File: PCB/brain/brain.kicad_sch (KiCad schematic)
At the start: 108 parts, among them J1 Screw_Terminal_01x02, J2 Conn_01x04, Q1 CSD17577Q3A, Q2 CSD17577Q3A, U1 ESP32-S3-WROOM-1, U10 MAX17049G+T10, U11 AP64501SP-13, U2 TMC2209-LA, U3 W5500, U4 MAX98357A, U5 USBLC6-2SC6, U6 AP2112K-3.3, U7 R5460N214AF-TR-FE, U8 CH221K, U9 BQ25792

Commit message: commit
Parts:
- added C48: 22uF, symbol Device:C
- added R27: 115k, Resistor_SMD:R_0603_1608Metric, symbol Device:R
- added R28: 22.1k, Resistor_SMD:R_0603_1608Metric, symbol Device:R
- C42: value 10uF -> 22uF
- C43: value 0.1uF -> 22uF
- L2: value L -> 3.6uH
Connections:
- net GND: now also R28.2
- net at C42.1, C43.1: now also C48.1
- net 5VHP: now reaches C42.2, C43.2
- net 5VHP: now also L2.2, C48.2, R27.1
- net at U11.5 (FB): now also R27.2, R28.1

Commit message: ethernet
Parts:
- removed U6: AP2112K-3.3, Package_TO_SOT_SMD:SOT-23-5, symbol Regulator_Linear:AP2112K-3.3
- added C49, C50, C57, C58: 22uF, symbol Device:C
- added C51, C56, C59, C62, C64, C65, C66, C67, C68, C69, C82: 0.1uF, symbol Device:C
- added C52, C53, C54, C55, C60, C61, C63, C81: 10uF, symbol Device:C
- added C70: 15pF, Capacitor_SMD:C_0603_1608Metric, symbol Device:C
- added C71: 15PF, Capacitor_SMD:C_0603_1608Metric, symbol Device:C
- added C72: 22nF, symbol Device:C
- added C73, C74: 6.8nF, symbol Device:C
- added C75, C76: 10nF, symbol Device:C
- added C77: 4.7uF, symbol Device:C
- added C78: 1nF/2kV, Capacitor_SMD:C_1206_3216Metric, symbol Device:C
- added FB1, FB2: FerriteBead, Inductor_SMD:L_0603_1608Metric, symbol Device:FerriteBead
- added FB3: CBW160808U601T, Inductor_SMD:L_0603_1608Metric, symbol Device:FerriteBead
- added J3: RJ45_Hanrun_HR911105A_Horizontal, Connector_RJ:RJ45_Hanrun_HR911105A_Horizontal, symbol Connector:RJ45_Hanrun_HR911105A_Horizontal
- added J4, J5, J6: Conn_01x04, Connector_JST:JST_XH_B4B-XH-A_1x04_P2.50mm_Vertical, symbol Connector_Generic:Conn_01x04
- added J7, J8: Conn_01x06, Connector_PinSocket_2.54mm:PinSocket_1x06_P2.54mm_Vertical, symbol Connector_Generic:Conn_01x06
- added JP1: Jumper_3_Open, Connector_PinHeader_2.54mm:PinHeader_1x03_P2.54mm_Vertical, symbol Jumper:Jumper_3_Open
- added L3, L4: 4.7uH, easyeda2kicad:IND-SMD_L5.0-W5.0, symbol Device:L
- added LS1: Speaker, symbol Device:Speaker
- added R29: 10k, Resistor_SMD:R_0603_1608Metric, symbol Device:R
- added R30: 1M, symbol Device:R
- added R31, R32, R34, R35: 49.9R, Resistor_SMD:R_0603_1608Metric, symbol Device:R
- added R33: 10R, Resistor_SMD:R_0603_1608Metric, symbol Device:R
- added R36, R37: 300R, Resistor_SMD:R_0603_1608Metric, symbol Device:R
- added R38: 12.4k, Resistor_SMD:R_0603_1608Metric, symbol Device:R
- added R39: 1M, Resistor_SMD:R_0603_1608Metric, symbol Device:R
- added U12: AP63205WU, Package_TO_SOT_SMD:TSOT-23-6, symbol Regulator_Switching:AP63205WU
- added U14: AP63203WU, Package_TO_SOT_SMD:TSOT-23-6, symbol Regulator_Switching:AP63203WU
- added Y1: 25MHz, Crystal:Crystal_SMD_3225-4Pin_3.2x2.5mm, symbol Device:Crystal_GND24
- C5, C6: value 10uF -> 220pF
- L2: value 3.6uH -> 3.3uH; footprint (none) -> easyeda2kicad:IND-SMD_L11.5-W10.0_SMMS1040; LCSC Part (none) -> C149592
- R27: value 115k -> 52.3k
- R28: value 22.1k -> 10k
- U3: LCSC Part (none) -> C32843
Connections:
- net +3.3V: now also U3.28 (VDD), C57.2, C58.2, C61.2, C62.2, C81.2, C82.2, FB3.1, J3.12, J3.9, J8.2 (Pin_2), J8.3 (Pin_3), JP1.1 (A), L4.2, R29.2, U14.1 (FB); no longer C5.2
- net +5V: now also C49.2, C50.2, J4.1 (Pin_1), J5.1 (Pin_1), J6.1 (Pin_1), JP1.3 (B), L3.2, U12.1 (FB); no longer C6.2, U5.5 (VBUS)
- net ALRT: now also R29.1
- net GND: now also C42.1, C43.1, C48.1, C5.2, C6.2, U3.14 (AGND), U3.16 (AGND), U3.19 (AGND), U3.29 (GND), U3.3 (AGND), U3.48 (AGND), U3.9 (AGND), U4.11 (GND), U4.15 (GND), U4.17 (PAD), U4.3 (GND), C49.1, C50.1, C52.1, C53.1, C54.1, C55.1, C57.1, C58.1, C59.2, C60.2, C61.1, C62.1, C63.1, C64.1, C65.1, C66.1, C67.1, C68.1, C69.1, C70.2, C71.2, C72.1, C75.1, C76.1, C77.1, C78.1, C81.1, C82.1, J3.8, J4.4 (Pin_4), J5.4 (Pin_4), J6.4 (Pin_4), J7.1 (Pin_1), J7.2 (Pin_2), J8.1 (Pin_1), R38.2, U12.4 (GND), U14.4 (GND), Y1.2 (G), Y1.4 (G); no longer C5.1, C6.1
- net SCL: now also J4.3 (Pin_3), J5.3 (Pin_3), J6.3 (Pin_3)
- net SDA: now also J4.2 (Pin_2), J5.2 (Pin_2), J6.2 (Pin_2)
- net VSYS: now also C52.2, C53.2, C54.2, C55.2, U12.3 (IN), U14.2 (EN), U14.3 (IN)
- net DIN: now reaches U4.1 (DIN)
- net at U4.10 (OUTN): now also FB2.1
- net LRCLK: now reaches U4.14 (LRCLK)
- net BCLK: now reaches U4.16 (BCLK)
- net at U4.4 (~{SD_MODE}): now also R30.1
- net AMP_VDD: now reaches U4.7 (VDD), U4.8 (VDD)
- net AMP_VDD: now also C59.1, C60.1, JP1.2 (C), R30.2
- net at U4.9 (OUTP): now also FB1.1
- net at U3.1 (TXN): now also J3.2 (TD-), R32.2
- net at U3.10 (EXRES1): now also R38.1
- net +3.3VA: now reaches U3.11 (AVDD), U3.15 (AVDD), U3.17 (AVDD), U3.21 (AVDD), U3.4 (AVDD), U3.8 (AVDD)
- net +3.3VA: now also C63.2, C64.2, C65.2, C66.2, C67.2, C68.2, C69.2, FB3.2, R31.1, R32.1, R33.1
- net at U3.2 (TXP): now also J3.1 (TD+), R31.2
- net at U3.20 (TOCAP): now also C77.2
- net at U3.22 (1V2O): now also C76.2
- net LINKLED: now reaches U3.25 (LINKLED)
- net LINKLED: now also R36.2
- net ACTLED: now reaches U3.27 (ACTLED)
- net ACTLED: now also R37.2
- net at U3.30 (XI/CLKIN): now also C71.1, R39.1, Y1.1
- net at U3.31 (XO): now also C70.1, R39.2, Y1.3
- net SCSn: now reaches U3.32 (~{SCS})
- net SCLK: now reaches U3.33 (SCLK)
- net SCLK: now also J7.4 (Pin_4)
- net MISO: now reaches U3.34 (MISO)
- net MISO: now also J8.6 (Pin_6)
- net MOSI: now reaches U3.35 (MOSI)
- net MOSI: now also J7.3 (Pin_3)
- net INTn: now reaches U3.36 (~{INT})
- net INTn: now also J7.6 (Pin_6)
- net RSTn: now reaches U3.37 (~{RST})
- net RSTn: now also J8.5 (Pin_5)
- net PMODE2: now reaches U3.43 (PMODE2)
- net PMODE1: now reaches U3.44 (PMODE1)
- net PMODE0: now reaches U3.45 (PMODE0)
- net at U3.5 (RXN): now also C74.2, R34.1
- net at U3.6 (RXP): now also C73.2, R35.1
- new net: C73.1, J3.3 (RD+)
- new net: C5.1, FB2.2, LS1.2
- new net: C75.2, J3.5 (RCT), R34.2, R35.2
- new net: C56.1, U14.6 (BST)
- new net: C56.2, L4.1, U14.5 (SW)
- new net: C51.2, L3.1, U12.5 (SW)
- new net: C51.1, U12.6 (BST)
- new net: C6.1, FB1.2, LS1.1
- new net: C74.1, J3.6 (RD-)
- new net: J3.10, R37.1
- new net: C72.2, J3.4 (TCT), R33.2
- new net: J3.11, R36.1
- new net 5V_EN: U12.2 (EN)
- new net CGND: C78.2, J3.SH
- new net EthCS: J7.5 (Pin_5)
- no-connect marks 6 -> 17
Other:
- note added: "3.3V Buck"
- note added: "5V Buck"
- note added: "5VHP Buck"
- note added: "Audio"
- note added: "Ethernet"
- note added: "Ethernet (FallBack)"
- note removed: "LDO"
- moved on the sheet: C4, C41, C42, C43, C44, C45, C46, C47, C48, D1, D2, D3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

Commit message: PCB/brain/
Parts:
- removed U5: USBLC6-2SC6, Package_TO_SOT_SMD:SOT-23-6, symbol Power_Protection:USBLC6-2SC6
- added C79: 22nF, symbol Device:C
- added C80, C83, C85, C87: 0.22uF, symbol Device:C
- added C84, C88: 10uF, symbol Device:C
- added C86: 22uF, easyeda2kicad:CAP-SMD_BD6.3-L6.6-W6.6-FD, symbol Device:C_Polarized
- added D10, D11, D6, D7, D8, D9: RED_LED, LED_SMD:LED_0603_1608Metric, symbol Device:LED
- added J9: Motor, easyeda2kicad:CONN-TH_4P-P2.54_MX128-2.54-GN01-04P-CU-Y-A, symbol Connector:Screw_Terminal_01x04
- added JP2: Jumper_3_Open, Connector_PinHeader_2.54mm:PinHeader_1x03_P2.54mm_Vertical, symbol Jumper:Jumper_3_Open
- added JP3: SolderJumper_2_Open, Jumper:SolderJumper-2_P1.3mm_Open_TrianglePad1.0x1.5mm, symbol Jumper:SolderJumper_2_Open
- added R40, R41: 1k, Resistor_SMD:R_0603_1608Metric, symbol Device:R
- added R42, R43: 6.8k, Resistor_SMD:R_0603_1608Metric, symbol Device:R
- added R44, R45: 0.05R, Resistor_SMD:R_1206_3216Metric, symbol Device:R
- added R46, R47, R48, R49, R50: 20k, Resistor_SMD:R_0603_1608Metric, symbol Device:R
- added R51: 33k, Resistor_SMD:R_0603_1608Metric, symbol Device:R
- added RV1: 10k, symbol Device:R_Potentiometer
- added U5: TPD2E2U06DCK, Package_TO_SOT_SMD:SOT-323_SC-70, symbol Power_Protection:TPD2E2U06DCK
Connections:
- net +3.3V: now also U2.15 (VCC_IO), C87.1, C88.2, JP3.1 (A), R48.1
- net +5V: now also JP2.3 (B)
- net 5VHP: now also D6.2 (A)
- net D+: now also U1.14 (USB_D+), U5.2
- net D-: now also U1.13 (USB_D-), U5.1
- net GND: now also U2.13 (CLK), U2.18 (GND), U2.25 (NC), U2.29 (GND), U2.3 (GND), C80.2, C84.1, C85.2, C86.2, C87.2, C88.1, D11.1 (K), R41.1, R42.1, R43.1, R44.2, R45.2, R46.2, R47.1, R49.2, RV1.3, U5.3
- net SCL: now also U1.17 (IO9)
- net SDA: now also U1.12 (IO8)
- net VBUS: now also D7.2 (A)
- net VSYS: now also D8.2 (A), JP2.1 (A)
- net OB2: now reaches U2.1 (OB2)
- net OB2: now also J9.4 (Pin_4)
- net MS2: now reaches U2.10 (MS2/AD1)
- net DIAG: now reaches U2.11 (DIAG)
- net INDEX: now reaches U2.12 (INDEX)
- net UART: now reaches U2.14 (~{PD}/UART)
- net STEP: now reaches U2.16 (STEP)
- net STEP: now also R47.2, R50.2
- net at U2.17 (VREF): now also RV1.2
- net DIR: now reaches U2.19 (DIR)
- net DIR: now also D10.2 (A), D9.1 (K)
- net EN: now reaches U2.2 (~{EN})
- net EN: now also R46.1
- net STDBY: now reaches U2.20 (STDBY)
- net OA2: now reaches U2.21 (OA2)
- net OA2: now also J9.2 (Pin_2)
- net VS: now reaches U2.22 (VS), U2.28 (VS)
- net VS: now also C80.1, C83.1, C85.1, C86.1, JP2.2 (C)
- net at U2.23 (BRA): now also R44.1
- net OA1: now reaches U2.24 (OA1)
- net OA1: now also J9.1 (Pin_1)
- net OB1: now reaches U2.26 (OB1)
- net OB1: now also J9.3 (Pin_3)
- net at U2.27 (BRB): now also R45.1
- net at U2.4 (CPO): now also C79.1
- net at U2.5 (CPI): now also C79.2
- net VCP: now reaches U2.6 (VCP)
- net VCP: now also C83.2
- net at U2.7 (SPREAD): now also JP3.2 (B)
- net at U2.8 (5VOUT): now also C84.2, R51.1
- net MS1: now reaches U2.9 (MS1/AD0)
- net at D1.2 (A): now also U1.25 (IO48)
- new net: D7.1 (K), R42.2
- new net: D8.1 (K), R43.2
- new net: D9.2 (A), R48.2
- new net: R51.2, RV1.1
- new net: R40.1, R41.2
- new net: D6.1 (K), R40.2
- new net: D10.1 (K), R49.1
- new net: D11.2 (A), R50.1
- no-connect marks 17 -> 20
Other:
- moved on the sheet: C37, C38, C39, C4, C40, C41, C42, C43, C44, C45, C46, C47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

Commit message: start working on esp32
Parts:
- removed C10, C11, C12, C13, C9: 0.1uF, symbol Device:C
- added C89: 10uF, symbol Device:C
- added C90: 1uF, symbol Device:C
- added J10: Conn_01x12, Connector_PinSocket_2.54mm:PinSocket_1x12_P2.54mm_Vertical, symbol Connector_Generic:Conn_01x12
- added R52: 10k, Resistor_SMD:R_0603_1608Metric, symbol Device:R
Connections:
- net +3.3V: now also C89.2, J10.4 (Pin_4), R52.1
- net DIAG: now also J10.11 (Pin_11)
- net DIR: now also J10.6 (Pin_6)
- net EN: now also U1.3 (EN), C90.2, J10.10 (Pin_10), R52.2
- net GND: now also C89.1, C90.1, J10.2 (Pin_2), J10.3 (Pin_3)
- net INDEX: now also J10.12 (Pin_12)
- net MS1: now also J10.8 (Pin_8)
- net MS2: now also J10.9 (Pin_9)
- net STEP: now also J10.5 (Pin_5)
- net UART: now also J10.7 (Pin_7)
- net VS: now also J10.1 (Pin_1)
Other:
- note added: "Motor Driver"
- moved on the sheet: C16, C79, C8, C80, C83, C84, C85, C86, C87, C88, D1, D10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

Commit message: brain sch done
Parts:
- removed RUN1: SW_Push, Button_Switch_SMD:SW_SPST_TS-1088-xR025, symbol Switch:SW_Push
- added BOOT, EN1: SW_Push, Button_Switch_SMD:SW_SPST_TS-1088-xR025, symbol Switch:SW_Push
- added C10, C11, C12, C13, C93: 10uF, symbol Device:C
- added C9, C92: 0.1uF, symbol Device:C
- added C91: 22uF, easyeda2kicad:CAP-SMD_BD6.3-L6.6-W6.6-FD, symbol Device:C_Polarized
- added J11: Conn_01x04, Connector_JST:JST_XH_B4B-XH-A_1x04_P2.50mm_Vertical, symbol Connector_Generic:Conn_01x04
- added JP4: Jumper_3_Open, Connector_PinHeader_2.54mm:PinHeader_1x03_P2.54mm_Vertical, symbol Jumper:Jumper_3_Open
- added R53, R54, R55, R56, R57: 10k, Resistor_SMD:R_0603_1608Metric, symbol Device:R
- added R58, R59: 100k, Resistor_SMD:R_0603_1608Metric, symbol Device:R
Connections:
- net PMODE0 is gone; now on net +3.3V: U3.45 (PMODE0)
- net PMODE1 is gone; now on net +3.3V: U3.44 (PMODE1)
- net PMODE2 is gone; now on net +3.3V: U3.43 (PMODE2)
- net SCSn is gone; now on net EthCS: U3.32 (~{SCS})
- net +3.3V: now also R4.1, JP4.1 (A), R53.1, R54.1, R55.1; no longer R4.2
- net +5V: now also C10.2, C11.2, C12.2, JP4.3 (B); no longer J1.1 (Pin_1)
- net 5VHP: now also J1.1 (Pin_1), C13.2, C91.1
- net 5VHP_EN: now also U1.38 (IO2), R59.1
- net 5V_EN: now also U1.39 (IO1), R58.1
- net ALRT: now also U1.35 (IO42)
- net BCLK: now also U1.32 (IO39)
- net CE: now also U1.6 (IO6)
- net DIAG: now also U1.31 (IO38)
- net DIN: now also U1.34 (IO41)
- net DIR: now also U1.10 (IO17)
- net EN: now also R4.2, U1.11 (IO18), EN1.2; no longer R52.2
- net EthCS: now also U1.18 (IO10), R53.2
- net GND: now also U3.23 (RSVD), BOOT.1, C10.1, C11.1, C12.1, C13.1, C9.1, C91.2, C92.1, C93.1, J11.4 (Pin_4), R56.2, R57.2, R58.2, R59.2
- net INT: no longer U9.21 (~{INT})
- net INTn: now also U1.22 (IO14), R54.2
- net LRCLK: now also U1.33 (IO40)
- net MISO: now also U1.21 (IO13)
- net MOSI: now also U1.19 (IO11)
- net MS1: now also R57.1
- net MS2: now also R56.1
- net RSTn: now also U1.8 (IO15), C92.2, R55.2
- net RX1: now also U1.4 (IO4), J11.2 (Pin_2); no longer U1.11 (IO18)
- net SCLK: now also U1.20 (IO12)
- net STEP: now also U1.9 (IO16)
- net TX1: now also U1.5 (IO5), J11.3 (Pin_3); no longer U1.10 (IO17)
- net UART: now also U1.23 (IO21)
- net BOOT: now reaches U1.27 (IO0)
- net BOOT: now also R52.2, BOOT.2
- net BQINT: now reaches U1.7 (IO7)
- net BQINT: now also U9.21 (~{INT})
- new net: C9.2, EN1.1
- new net: C93.2, J11.1 (Pin_1), JP4.2 (C)
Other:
- note added: "ESP32"
- note added: "Modules"
- moved on the sheet: BT1, BT2, C1, C14, C15, C16, C17, C18, C19, C2, C20, C21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

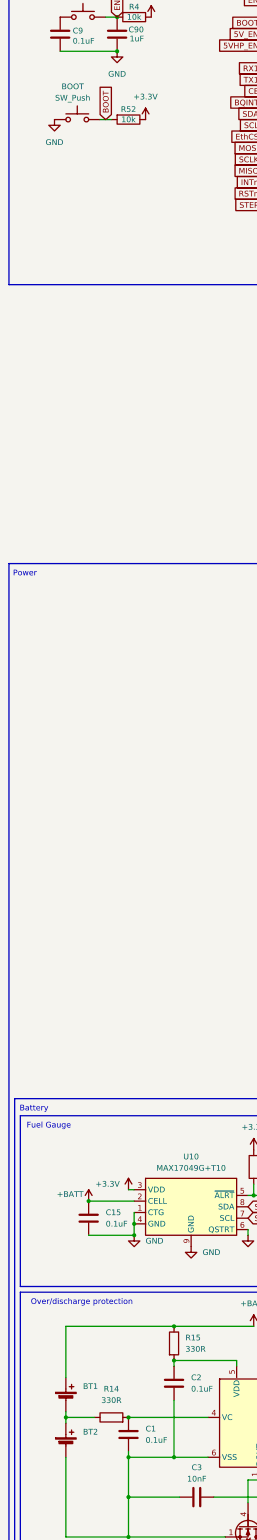
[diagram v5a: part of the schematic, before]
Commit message: add footprints to BrainPCB
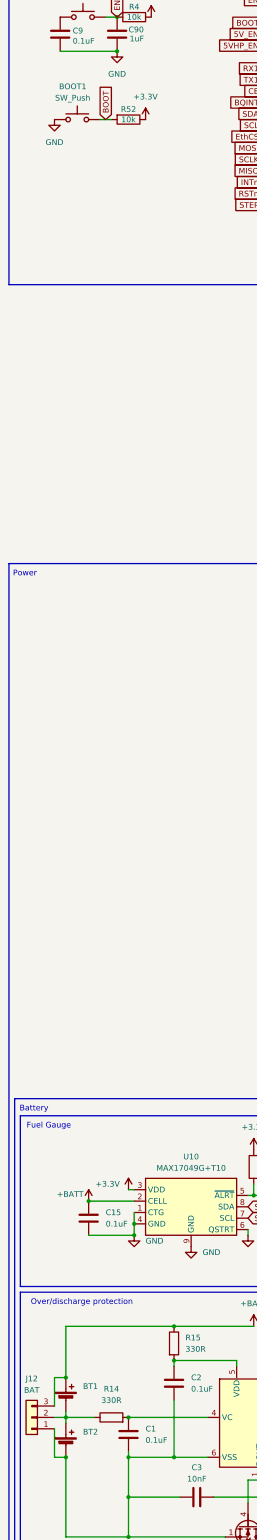
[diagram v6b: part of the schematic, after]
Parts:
- added J12: BAT, Connector_JST:JST_XH_B3B-XH-A_1x03_P2.50mm_Vertical, symbol Connector_Generic:Conn_01x03
- BT1, BT2, TH1: footprint (none) -> Connector_PinHeader_2.54mm:PinHeader_1x02_P2.54mm_Vertical
- C1, C10, C11, C12, C13, C14, C15, C16, C2, C24, C25, C28, C29, C3, C30, C31, C32, C36, C4, C40, C44, C45, C46, C47, C5, C51, C56, C59, C6, C60, C61, C62, C63, C64, C65, C66, C67, C68, C69, C7, C72, C73, C74, C75, C76, C77, C79, C8, C80, C81, C82, C83, C84, C85, C87, C88, C89, C9, C90, C92, C93: footprint (none) -> Capacitor_SMD:C_0603_1608Metric
- C17, C18, C19, C20, C21, C22, C23, C26, C27, C33, C34, C35, C37, C38, C39, C41, C52, C53, C54, C55: footprint (none) -> Capacitor_SMD:C_0603_1608Metric; LCSC Part (none) -> C194427
- C42: footprint (none) -> Capacitor_SMD:C_0805_2012Metric; LCSC Part (none) -> C162295
- C43, C48, C49, C50, C57, C58: footprint (none) -> Capacitor_SMD:C_0805_2012Metric
- L1: footprint (none) -> easyeda2kicad:IND-SMD_L7.1-W6.5-P5.60
- LS1: footprint (none) -> Connector_JST:JST_XH_B2B-XH-AM_1x02_P2.50mm_Vertical
- R23, R30: footprint (none) -> Resistor_SMD:R_0603_1608Metric
- RV1: footprint (none) -> easyeda2kicad:RES-ADJ-SMD_3P-L3.8-W3.7_VGF39NCHXT; LCSC Part (none) -> C22461454
- U1: LCSC Part (none) -> C2913199
- renumbered BOOT to BOOT1
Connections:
- net +BATT: now also J12.3 (Pin_3)
- net at BT2.2 (-), C1.2, C2.2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: now also J12.1 (Pin_1)
- net at BT1.2 (-), BT2.1 (+), R14.1: now also J12.2 (Pin_2)

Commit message: start pcb routing
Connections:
- net +3.3V: no longer U3.43 (PMODE2), U3.44 (PMODE1), U3.45 (PMODE0)
- net OA1: now also J9.2 (Pin_2); no longer J9.1 (Pin_1)
- net OA2: now also J9.1 (Pin_1); no longer J9.2 (Pin_2)
- new net PMODE0: U3.45 (PMODE0)
- new net PMODE1: U3.44 (PMODE1)
- new net PMODE2: U3.43 (PMODE2)

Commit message: more pcb routing
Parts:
- added C94: 22uF, Capacitor_SMD:C_0805_2012Metric, symbol Device:C
- C25, C28, C36, C40, C59, C62, C64, C65, C66, C67, C68, C69, C8: footprint Capacitor_SMD:C_0603_1608Metric -> Capacitor_SMD:C_0402_1005Metric; LCSC Part (none) -> C77020
- C82, C9: footprint Capacitor_SMD:C_0603_1608Metric -> Capacitor_SMD:C_0402_1005Metric
- U11: footprint easyeda2kicad:SOIC-8_L4.9-W3.9-P1.27-LS6.0-BL-EP-1 -> Package_SO:SOIC-8-1EP_3.9x4.9mm_P1.27mm_EP2.29x3mm_ThermalVias
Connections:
- net GND: now also C94.1
- net VSYS: now also C94.2
- net SW1: now reaches C31.1, L1.1, U9.28 (SW1)
- net SW2: now reaches C30.2, L1.2, U9.26 (SW2)
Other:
- moved on the sheet: C41
